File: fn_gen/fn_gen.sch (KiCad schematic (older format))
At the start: 7 parts, among them U1 LM741

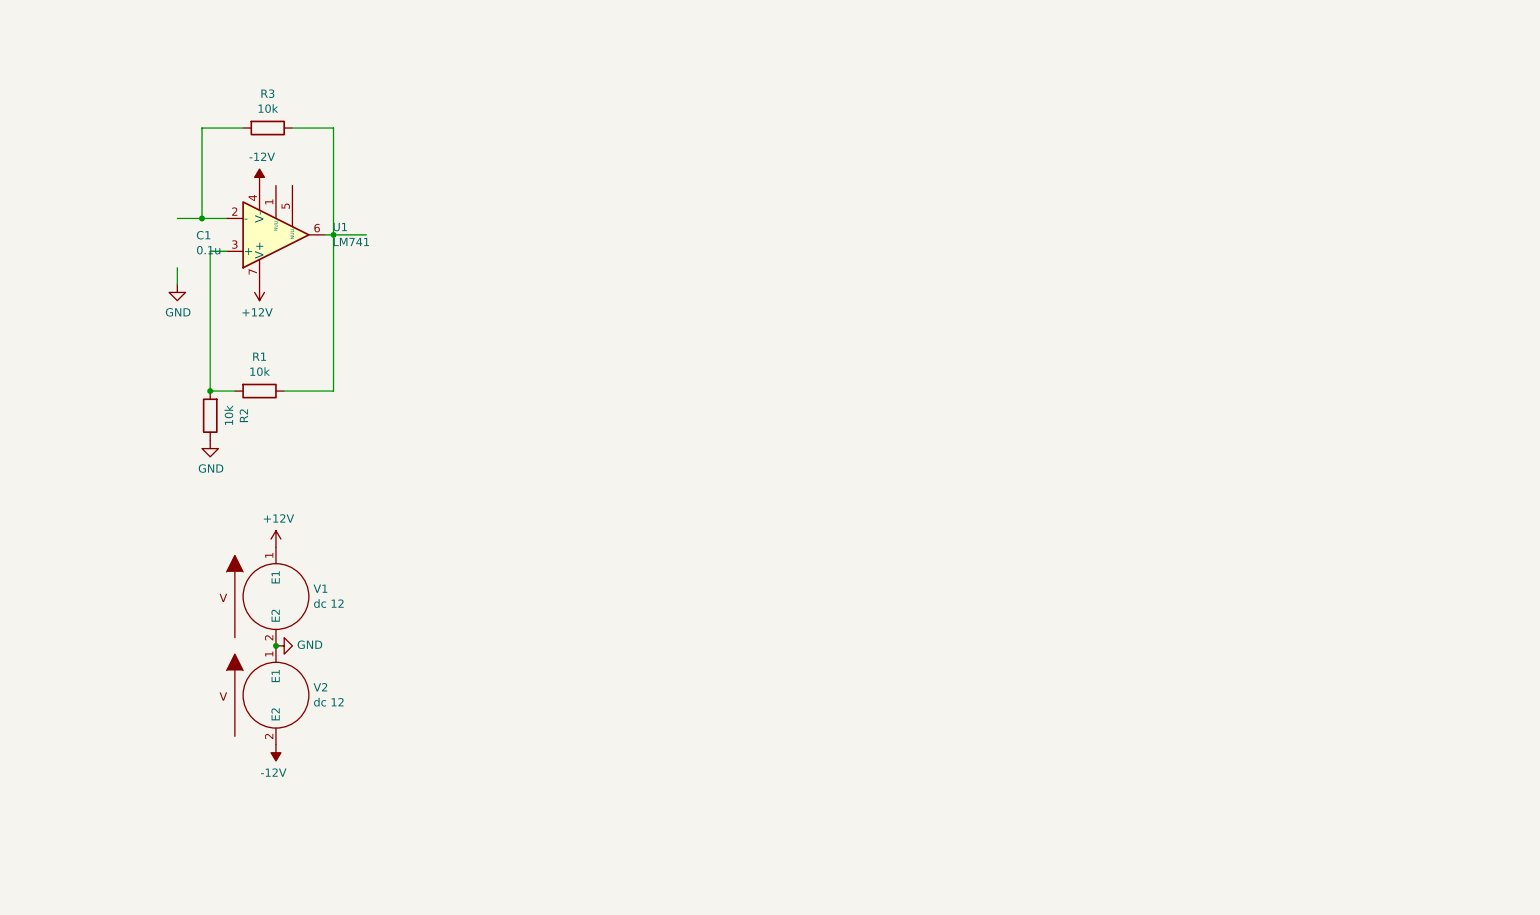
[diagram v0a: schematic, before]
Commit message: Implement basic function generator with Wein bridge oscillator
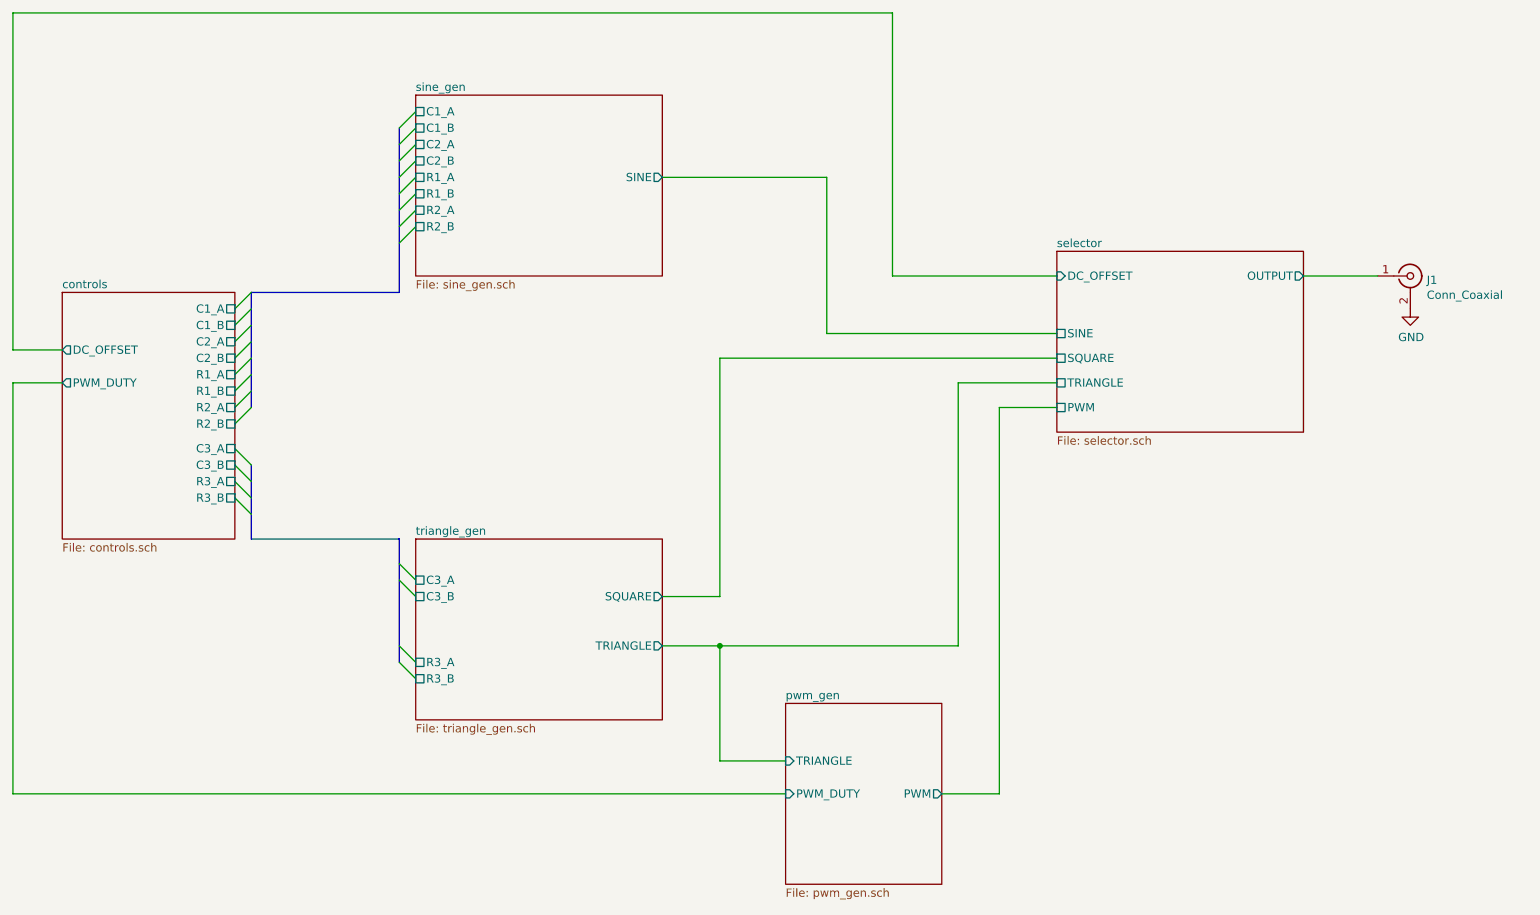
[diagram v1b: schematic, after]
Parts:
- removed C1: 0.1u, symbol Device:C
- removed R1, R2, R3: 10k, symbol Device:R
- removed U1: LM741, symbol Amplifier_Operational:LM741
- removed V1, V2: dc 12, symbol pspice:VSOURCE
- added J1: Conn_Coaxial, symbol Connector:Conn_Coaxial
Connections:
- net labels removed: +12V, -12V
- wire segments 14 -> 24
